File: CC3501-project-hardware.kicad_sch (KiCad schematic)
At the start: 18 parts, among them J1 USB_C_Receptacle_USB2.0_16P, Q1 AO3400A, U1 RP2040, U3 CR2013-MI2120, U4 SY8089A1AAC, U7 HX711

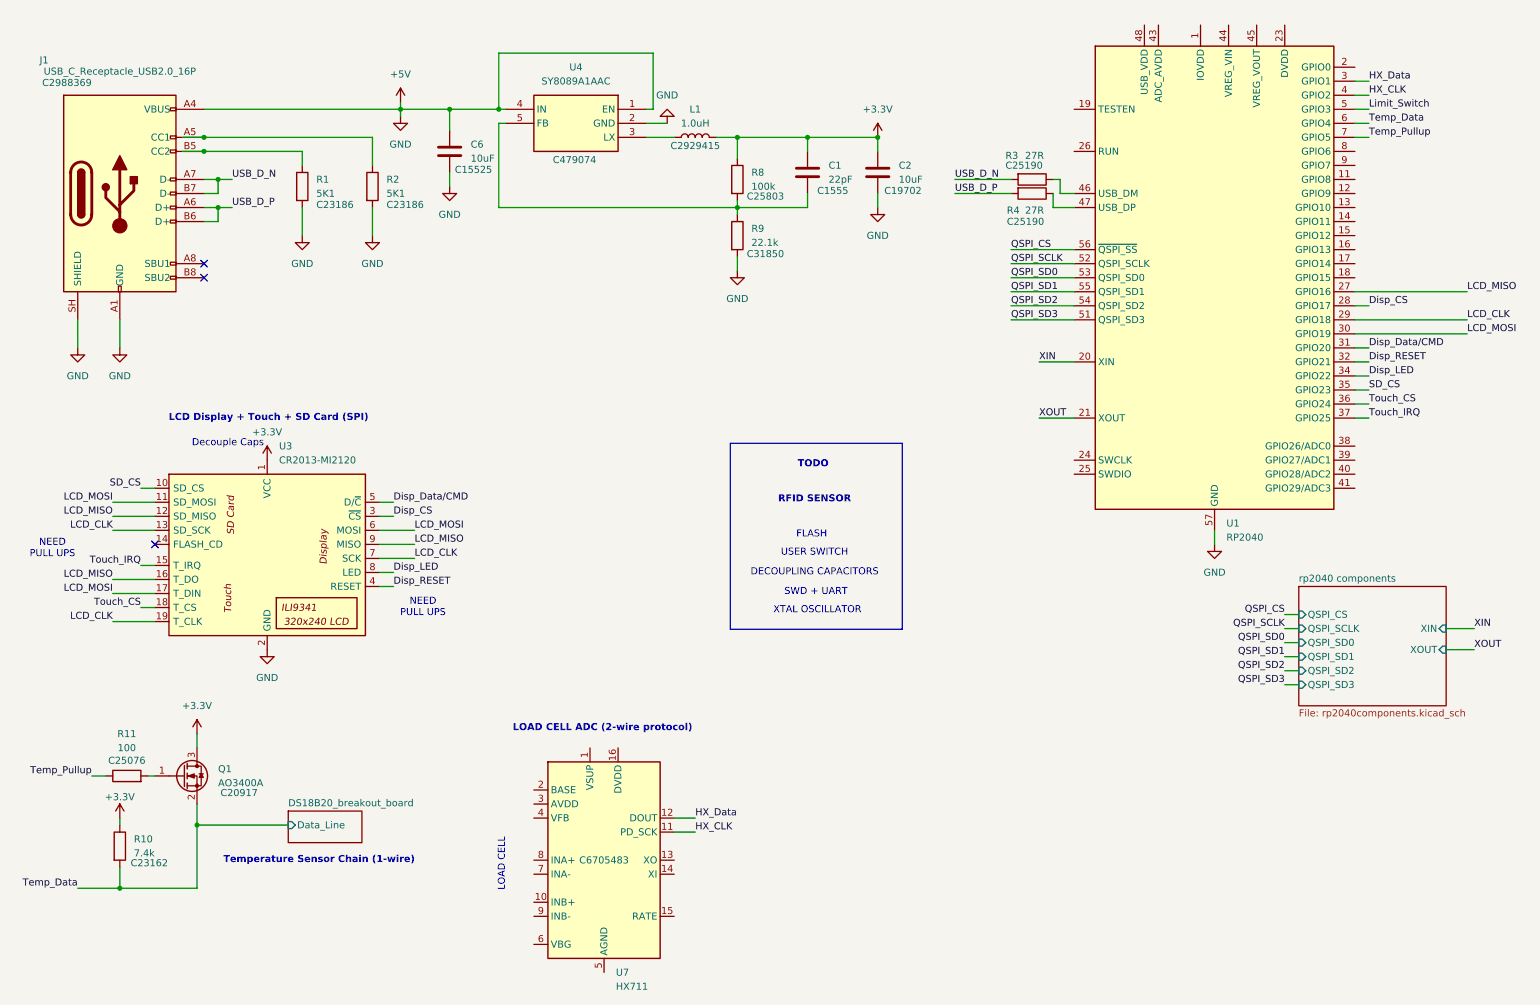
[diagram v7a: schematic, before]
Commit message: add a whole bunch off stuff
- separated TFT display and HX711 into separate pages
- add ESD protection resistor to temp sensor
- corrected/added various JLC PCB part numbers
- swapped oscillator for the one used in part 1
- moved blocks of schematic around and into other pages to neaten it all up
- added file with download footprints, symbols, and 3D models
- add decoupling caps for RP2040
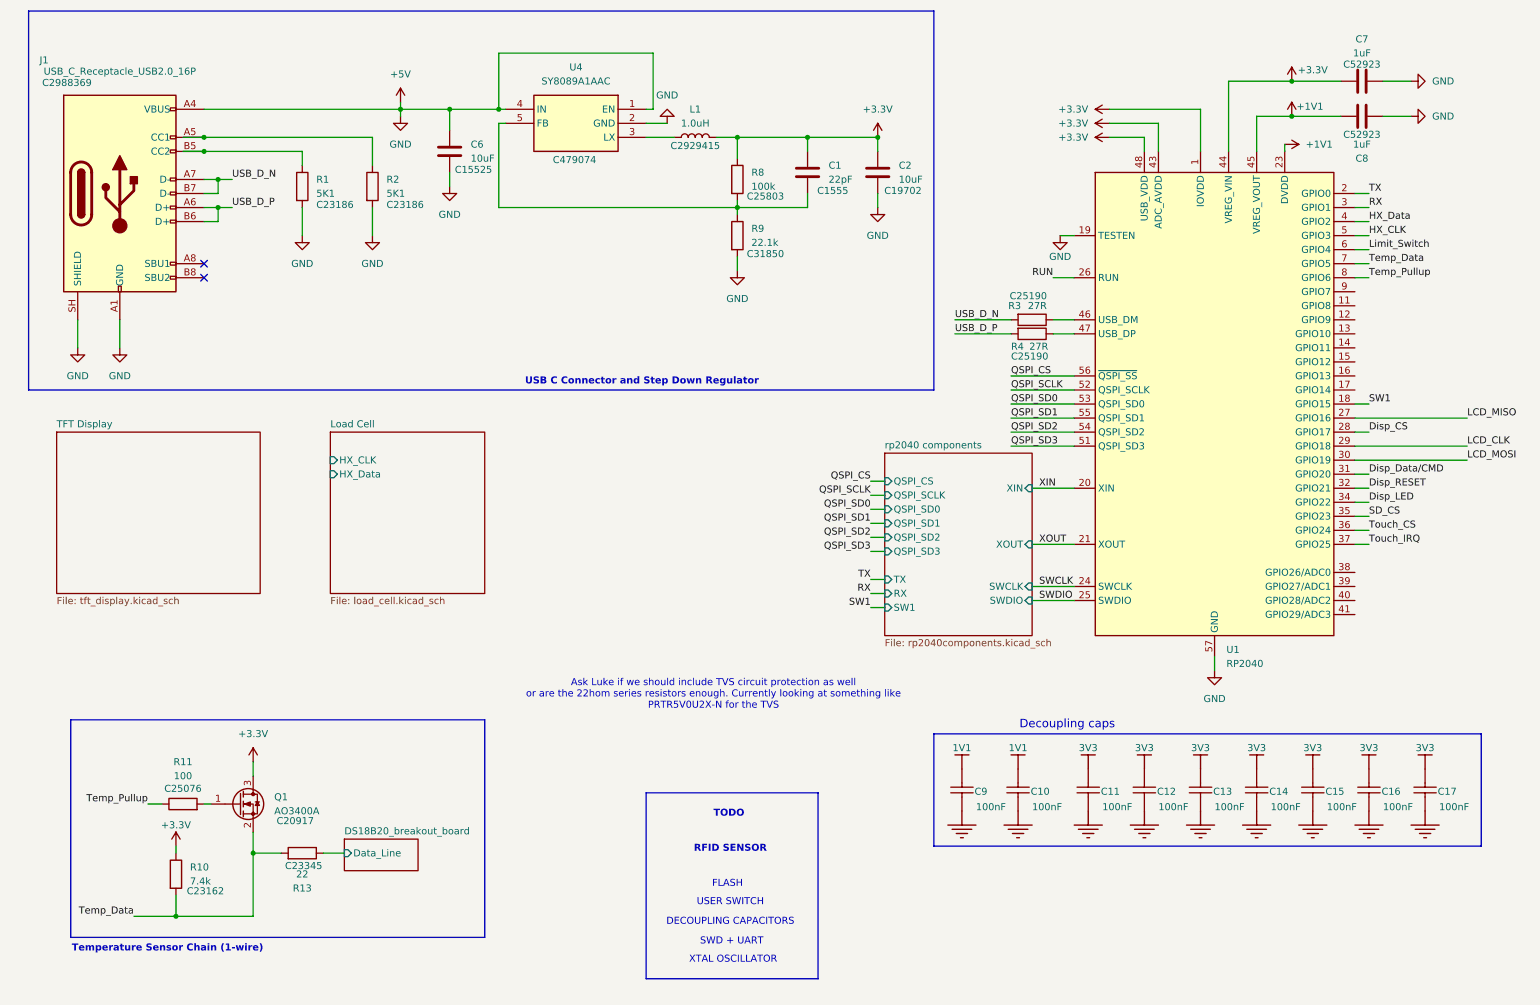
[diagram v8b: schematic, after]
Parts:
- removed U3: CR2013-MI2120, Display:CR2013-MI2120, symbol Driver_Display:CR2013-MI2120
- removed U7: HX711, Package_SO:SOIC-16_3.9x9.9mm_P1.27mm, symbol Analog_ADC:HX711
- added C10, C11, C12, C13, C14, C15, C16, C17, C9: CL05B104KO5NNNC, Capacitor_SMD:C_0402_1005Metric, symbol James Cook University:root_1_CAP-NP-2_James Cook University
- added C7, C8: 1uF, Capacitor_SMD:C_0402_1005Metric, symbol Device:C
- added R13: 22, Resistor_SMD:R_0603_1608Metric, symbol Device:R
- J1: LCSC PN (none) -> C2988369; LSCS PN C2988369 -> (none)
- R1, R2: LCSC PN (none) -> C23186; LSCS PN C23186 -> (none)
- R3, R4: LCSC PN (none) -> C25190; LSCS PN C25190 -> (none)
- U1: LCSC PN (none) -> C2040
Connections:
- net +3.3V: now also U1.1 (IOVDD), U1.10 (IOVDD), U1.22 (IOVDD), U1.33 (IOVDD), U1.42 (IOVDD), U1.43 (ADC_AVDD), U1.44 (VREG_VIN), U1.48 (USB_VDD), U1.49 (IOVDD), C7.2
- net +5V: now also U1.19 (TESTEN), C10.1, C11.1, C12.1, C13.1, C14.1, C15.1, C16.1, C17.1, C7.1, C8.2, C9.1
- net HX_CLK: now also U1.5 (GPIO3); no longer U1.4 (GPIO2)
- net HX_Data: now also U1.4 (GPIO2); no longer U1.3 (GPIO1)
- net Limit_Switch: now also U1.6 (GPIO4); no longer U1.5 (GPIO3)
- net Temp_Data: now also U1.7 (GPIO5), R13.2; no longer U1.6 (GPIO4)
- net Temp_Pullup: now also U1.8 (GPIO6); no longer U1.7 (GPIO5)
- net SW1: now reaches U1.18 (GPIO15)
- net TX: now reaches U1.2 (GPIO0)
- net +1V1: now reaches U1.23 (DVDD), U1.50 (DVDD)
- net +1V1: now also U1.45 (VREG_VOUT), C8.1
- net SWCLK: now reaches U1.24 (SWCLK)
- net SWDIO: now reaches U1.25 (SWDIO)
- net RUN: now reaches U1.26 (RUN)
- new net 1V1: C10.2, C9.2
- new net 3V3: C11.2, C12.2, C13.2, C14.2, C15.2, C16.2, C17.2
- new net DS18B20_breakout_board/Data_Line: R13.1
- new net RX: U1.3 (GPIO1)
- no-connect marks 3 -> 2
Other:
- added sheet Load Cell (load_cell.kicad_sch)
- added sheet TFT Display (tft_display.kicad_sch)
- sheet rp2040 components ports: added RX, SW1, SWCLK, SWDIO, TX; removed none
- note added: "Ask Luke if we should include TVS circuit protection as well or are the 22hom series resistors enough. Currently looking at something like PRTR5V0U2X-N for the TVS"
- note added: "Decoupling caps"
- note added: "USB C Connector and Step Down Regulator"
- note removed: "Decouple Caps"
- note removed: "LCD Display + Touch + SD Card (SPI)"
- note removed: "LOAD CELL"
- note removed: "LOAD CELL ADC (2-wire protocol)"
- note removed: "NEED PULL UPS"
- moved on the sheet: Q1, R10, R11, R3, R4, U1
